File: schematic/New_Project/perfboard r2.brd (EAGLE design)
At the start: 50.8 x 27.9 mm, 16 parts

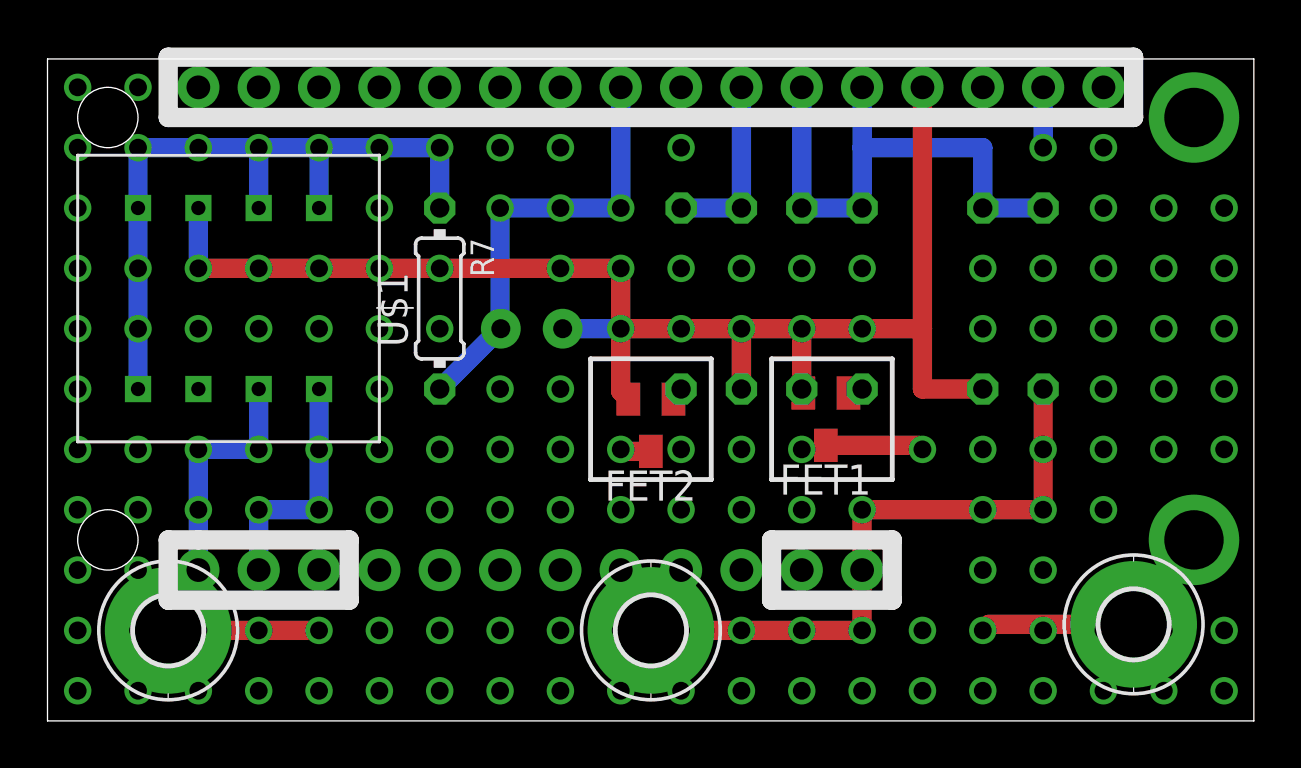
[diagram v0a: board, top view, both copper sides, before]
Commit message: Fix perfboard wiring
No, A2 isnt supposed to drive PWM too -><-
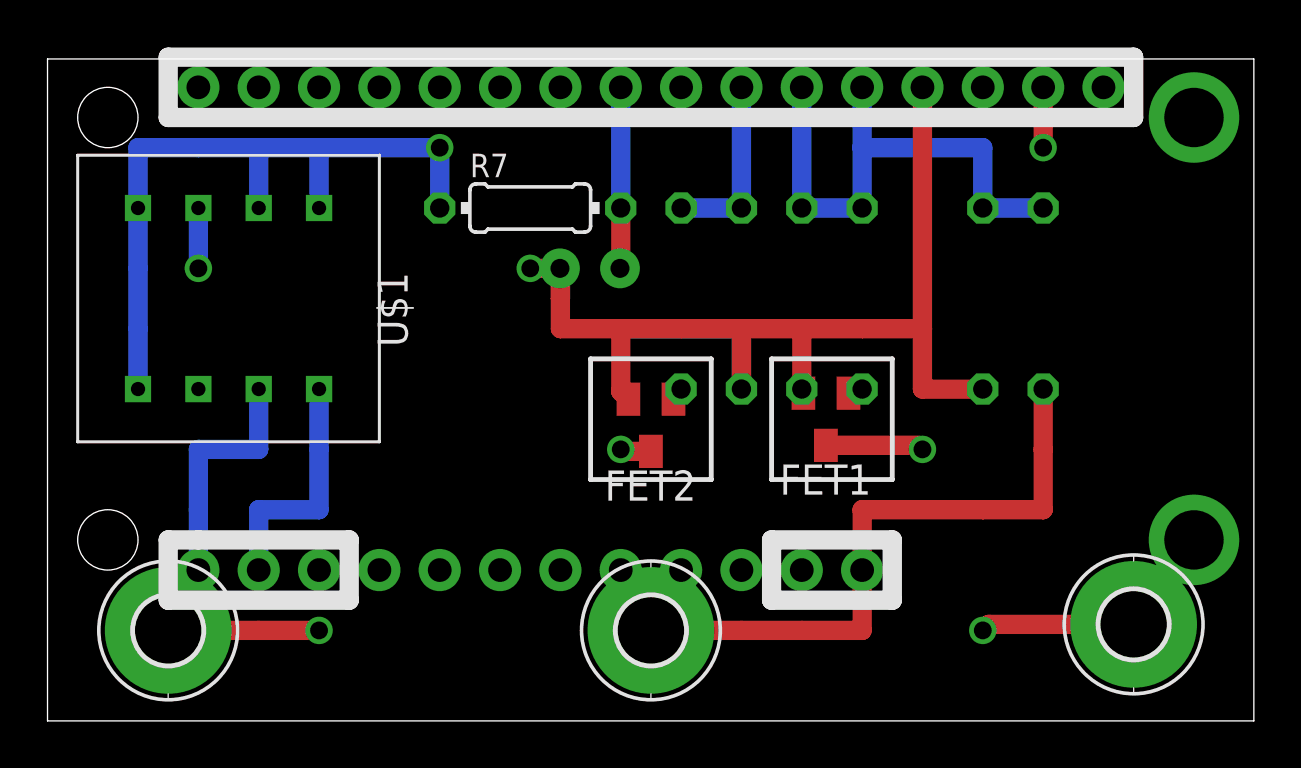
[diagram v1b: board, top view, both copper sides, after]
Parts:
- moved R7 5.39 mm to (19.1, 20.3), turned to 0 degrees
- moved R6 3.59 mm to (21.6, 17.8), turned to 0 degrees
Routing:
- net PHOTO: track 18.8 -> 7.63 mm, vias 3 -> 0
- net GND: track 69.2 -> 68.1 mm, vias 12 -> 2
- net 3.3V: vias 12 -> 2
- net VBAT: vias 8 -> 0
- net SDA: vias 3 -> 0
- net SCL: vias 3 -> 0
- net N$3: vias 9 -> 2
- net N$1: vias 3 -> 2

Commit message: Reorg perfboard
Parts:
- R7: value 100k -> 10k
- moved FET2 2.54 mm to (26.7, 11.2)
- moved R2 2.54 mm to (27.9, 16.5)
- moved R3 2.54 mm to (25.4, 16.5)
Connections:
- net 3.3V: now also R6.2; no longer R7.1
- net GND: now also R7.1; no longer R6.2
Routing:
- net GND: track 68.1 -> 62.3 mm, vias 2 -> 0
- net 3.3V: track 58.4 -> 63.5 mm, vias 2 -> 3
- net N$3: track 26.5 -> 29.0 mm
- net BATT_SENSE: track 15.2 -> 12.7 mm
